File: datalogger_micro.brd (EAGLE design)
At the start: 32 x 40.6 mm, 46 parts, among them IC1 DS3231/SO, IC2 LD117AS33TR, M1 PAT, M2 PAT, Q2 IRLML5203

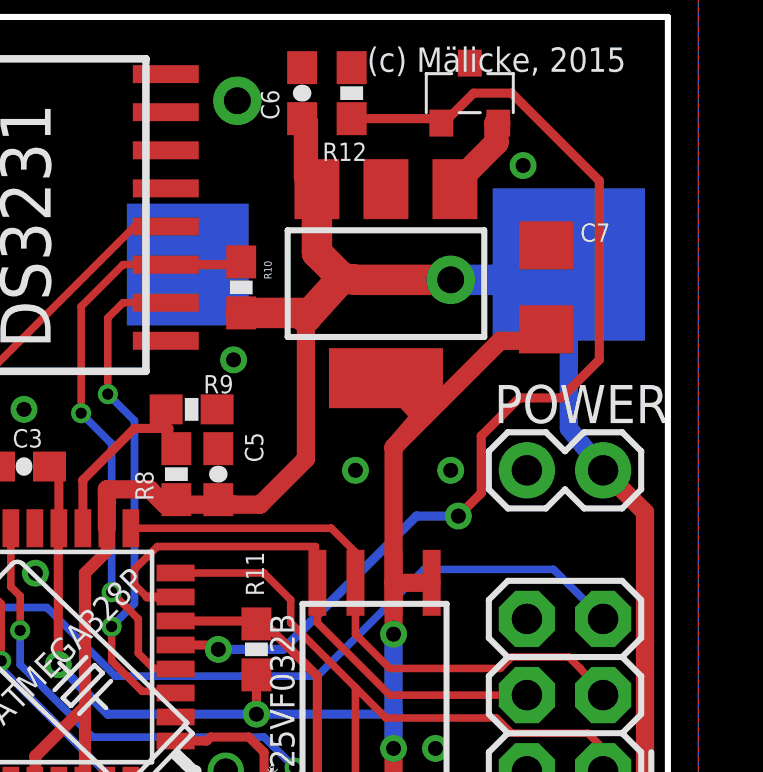
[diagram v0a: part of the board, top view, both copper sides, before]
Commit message: layout error bugfixes
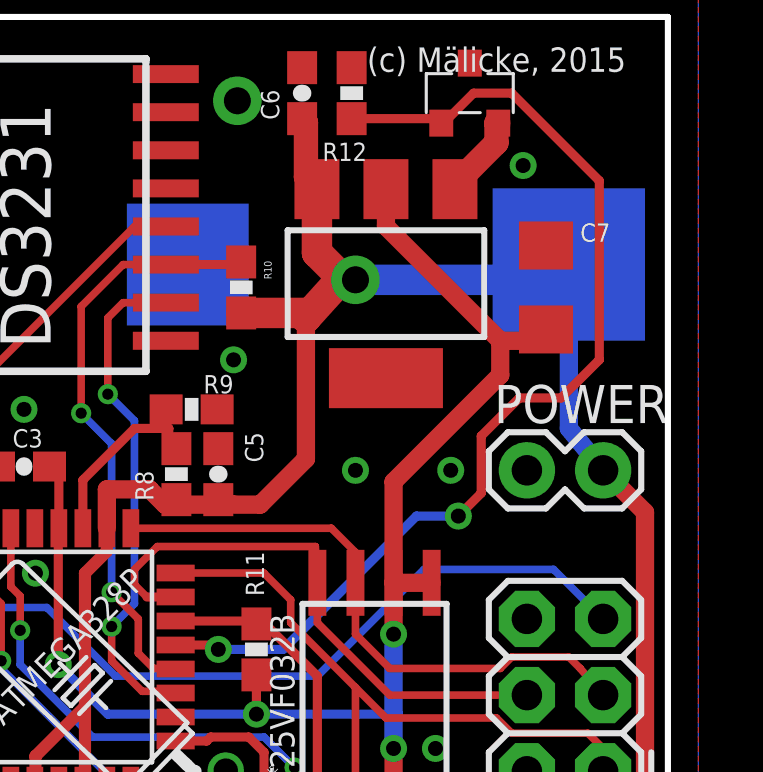
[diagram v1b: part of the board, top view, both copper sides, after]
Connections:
- net VCC-ST: now also IC2.2; no longer IC2.4
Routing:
- net VCC-ST: track 77.0 -> 80.6 mm
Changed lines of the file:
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@@
 <contactref element="R13" pad="1"/>
 <contactref element="R11" pad="1"/>
-<contactref element="IC2" pad="4"/>
+<contactref element="IC2" pad="2"/>
 <contactref element="R18" pad="2"/>
 <contactref element="ATMEGA328P" pad="20"/>
@@
 <wire x1="34.798" y1="9.144" x2="35.179" y2="9.271" width="0.3048" layer="1"/>
 <wire x1="35.179" y1="9.271" x2="35.1481875" y2="9.564" width="0.3048" layer="1"/>
-<wire x1="27.813" y1="23.682" x2="27.813" y2="28.194" width="0.6096" layer="1"/>
-<wire x1="27.813" y1="28.194" x2="31.369" y2="31.75" width="0.6096" layer="1"/>
 <wire x1="31.369" y1="31.75" x2="32.642" y2="31.75" width="0.6096" layer="1"/>
 <wire x1="32.642" y1="31.75" x2="32.893" y2="32.128" width="0.6096" layer="1"/>
-<wire x1="27.813" y1="28.194" x2="28.702" y2="29.235" width="0.6096" layer="1"/>
-<wire x1="28.702" y1="29.235" x2="27.559" y2="30.505" width="0.6096" layer="1"/>
 <wire x1="15.367" y1="7.577" x2="16.51" y2="8.636" width="0.6096" layer="1"/>
 <wire x1="16.51" y1="8.636" x2="27.813" y2="8.636" width="0.6096" layer="1"/>
@@
 <wire x1="16.656" y1="27.882" x2="16.344" y2="27.57" width="0.3048" layer="1"/>
 <wire x1="16.344" y1="27.57" x2="16.344" y2="27.559" width="0.3048" layer="1"/>
+<wire x1="27.559" y1="36.805" x2="27.559" y2="35.56" width="0.6096" layer="1"/>
+<wire x1="27.559" y1="35.56" x2="31.369" y2="31.75" width="0.6096" layer="1"/>
+<wire x1="31.369" y1="31.75" x2="31.369" y2="30.607" width="0.6096" layer="1"/>
+<wire x1="31.369" y1="30.607" x2="27.813" y2="27.051" width="0.6096" layer="1"/>
+<wire x1="27.813" y1="27.051" x2="27.813" y2="23.682" width="0.6096" layer="1"/>
 <wire x1="16.637" y1="25.4826" x2="16.656" y2="25.5016" width="0" layer="19" extent="1-1"/>
 <wire x1="27.813" y1="15.875" x2="27.813" y2="15.942" width="0" layer="19" extent="1-1"/>
@@
 <wire x1="25.259" y1="34.685" x2="26.0985" y2="33.8455" width="1.016" layer="1"/>
 <wire x1="26.0985" y1="33.8455" x2="26.543" y2="33.782" width="1.016" layer="1"/>
-<wire x1="26.543" y1="33.782" x2="29.718" y2="33.782" width="1.016" layer="1"/>
-<via x="29.718" y="33.782" extent="1-16" drill="0.9"/>
-<wire x1="29.718" y1="33.782" x2="33.147" y2="33.782" width="1.016" layer="16"/>
+<via x="26.543" y="33.782" extent="1-16" drill="0.9"/>
+<wire x1="26.543" y1="33.782" x2="33.147" y2="33.782" width="1.016" layer="16"/>
 <wire x1="33.147" y1="33.782" x2="33.655" y2="34.29" width="1.016" layer="16"/>
 <wire x1="22.733" y1="32.678" x2="24.931" y2="32.678" width="1.016" layer="1"/>

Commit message: MOSFET fix
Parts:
- added R19: 100k, SparkFun:0603-RES
- moved M1 17.0 mm to (23.4, 6.60)
- moved M2 17.0 mm to (6.35, 6.48)
- moved VD1 17.0 mm to (25.9, 4.06)
- moved VD2 17.0 mm to (8.89, 3.94)
- moved R12 12.3 mm to (35.1, 31.2)
- moved C6 8.49 mm to (31.8, 35.2)
- moved Q2 8.30 mm to (31.2, 31.8), turned to 90 degrees
- moved C7 6.87 mm to (26.4, 31.2), turned to 180 degrees
- moved R9 5.11 mm to (16.5, 27.2), turned to 270 degrees
- moved R3 4.97 mm to (12.1, 7.90)
- moved IC2 3.97 mm to (27.1, 37.6), turned to 0 degrees
- moved C5 3.27 mm to (18.8, 28.1), turned to 0 degrees
- moved C2 2.93 mm to (9.88, 13.1), turned to 180 degrees
- moved R11 2.11 mm to (22.1, 19.7)
- moved 32.768KHZ 2.11 mm to (20.2, 14.7)
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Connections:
- removed net N$1: IC2.1, Q2.2
- new net N$10: C6.1, IC2.3, Q2.3
- new net N$11: Q2.1, R12.1, R19.2
- net GND: now also IC2.1; no longer Q2.3, R12.2
- net N$5: now also M2.1; no longer M1.1
- net N$6: now also M1.1; no longer M2.1
- net N$8: now also M2.2; no longer M1.2
- net N$9: now also M1.2; no longer M2.2
- net VBAT: now also Q2.2, R19.1; no longer C6.1, IC2.3
- net VCC/ST_ON: now also R12.2; no longer Q2.1, R12.1
- net VDIV1: now also VD1.2; no longer VD2.2
- net VDIV2: now also VD2.2; no longer VD1.2
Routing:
- net VBAT: track 144.4 -> 132.6 mm
- net VCC/ST_ON: track 35.5 -> 24.6 mm
- net DTR: track 8.76 -> 2.52 mm, vias 1 -> 0
- net N$10: track 0.00 -> 6.05 mm
- net VCC-ST: track 80.6 -> 77.1 mm
- net N$11: track 0.00 -> 2.96 mm
- net N$1: track 2.90 -> 0.00 mm
- net RTC_VCC: track 16.8 -> 19.4 mm
- net RTC_RST: track 13.8 -> 16.2 mm
- net VDIV2: track 30.8 -> 28.6 mm
- net SCK: track 20.0 -> 22.1 mm
- net A6: track 6.63 -> 4.54 mm
- net SOIL2: track 23.4 -> 21.4 mm
- net TXO: track 7.61 -> 5.65 mm
- net MOSI: track 18.9 -> 20.8 mm
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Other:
- board text added: "Version 0.96"
- board text removed: "Version 0.95"

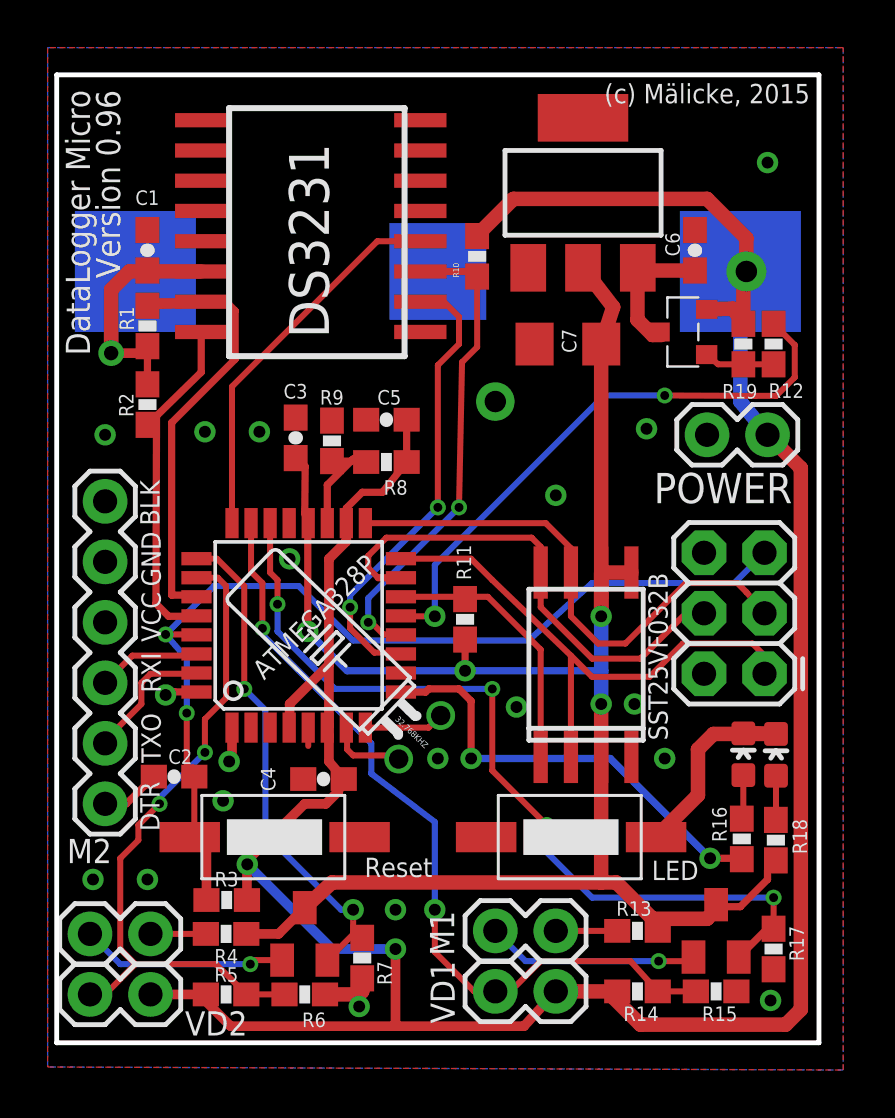
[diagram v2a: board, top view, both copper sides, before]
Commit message: SST25 Layout
pins 5-8 were switched
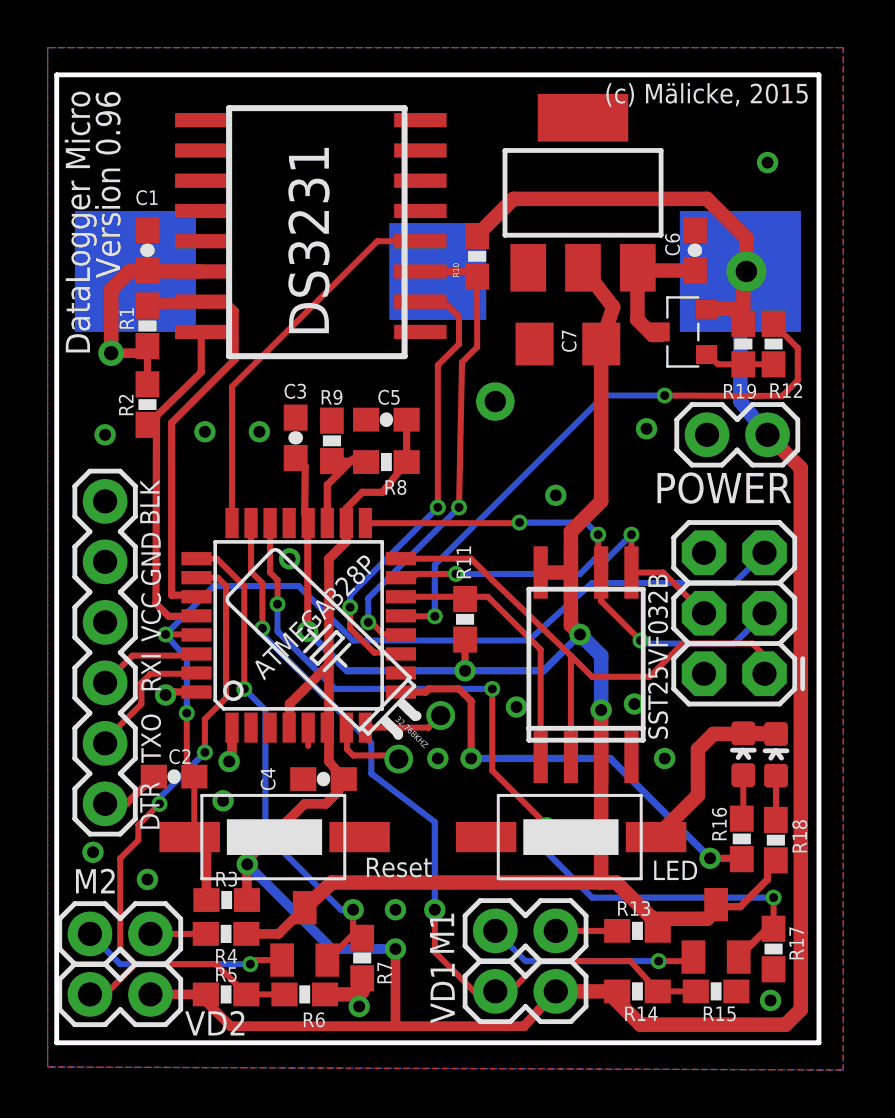
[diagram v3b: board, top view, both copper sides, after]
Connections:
- net MOSI: now also U$3.5; no longer U$3.8
- net SCK: now also U$3.6; no longer U$3.7
- net VCC-ST: now also U$3.7, U$3.8; no longer U$3.5, U$3.6
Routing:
- net MOSI: track 20.8 -> 15.8 mm, vias 0 -> 2
- net SCK: track 22.1 -> 21.0 mm, vias 0 -> 3
- net VCC-ST: track 77.1 -> 76.4 mm
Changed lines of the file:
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@@
 <?xml version="1.0" encoding="utf-8"?>
 <!DOCTYPE eagle SYSTEM "eagle.dtd">
-<eagle version="7.2.0">
+<eagle version="7.3.0">
 <drawing>
 <settings>
@@
 </element>
 <element name="M2" library="SparkFun" package="1X02" value="PAT" x="6.35" y="6.477" smashed="yes">
-<attribute name="NAME" x="5.3848" y="9.4488" size="1.016" layer="25" ratio="10"/>
+<attribute name="NAME" x="5.6388" y="8.1788" size="1.016" layer="25" ratio="10"/>
 <attribute name="VALUE" x="5.08" y="3.302" size="1.27" layer="27"/>
 </element>
@@
 <via x="25.908" y="24.892" extent="1-16" drill="0.5" diameter="0.254"/>
 <contactref element="SPI" pad="6"/>
-<via x="6.477" y="8.763" extent="1-16" drill="0.5" diameter="0.254"/>
+<via x="6.477" y="9.906" extent="1-16" drill="0.5" diameter="0.254"/>
 <wire x1="15.494" y1="15.1574" x2="15.513" y2="15.1384" width="0.254" layer="1"/>
 <via x="11.176" y="27.559" extent="1-16" drill="0.5" diameter="0.254"/>
@@
 </signal>
 <signal name="SCK">
-<contactref element="U$3" pad="7"/>
+<contactref element="U$3" pad="6"/>
 <contactref element="ATMEGA328P" pad="17"/>
-<wire x1="17.913" y1="23.7236" x2="25.4854" y2="23.7236" width="0.254" layer="1"/>
 <contactref element="SPI" pad="3"/>
-<wire x1="34.671" y1="19.939" x2="33.909" y2="20.828" width="0.254" layer="1"/>
-<wire x1="33.909" y1="20.828" x2="33.528" y2="21.209" width="0.254" layer="1"/>
-<wire x1="33.528" y1="21.209" x2="31.369" y2="21.209" width="0.254" layer="1"/>
-<wire x1="31.369" y1="21.209" x2="28.829" y2="18.669" width="0.254" layer="1"/>
-<wire x1="28.829" y1="18.669" x2="27.686" y2="18.669" width="0.254" layer="1"/>
-<wire x1="27.686" y1="18.669" x2="26.543" y2="19.812" width="0.254" layer="1"/>
-<wire x1="26.543" y1="19.812" x2="26.543" y2="21.65" width="0.254" layer="1"/>
-<wire x1="25.4854" y1="23.7236" x2="26.543" y2="22.666" width="0.254" layer="1"/>
-<wire x1="26.543" y1="22.666" x2="26.543" y2="21.65" width="0.254" layer="1"/>
+<wire x1="17.913" y1="23.7236" x2="24.3586" y2="23.7236" width="0.254" layer="1"/>
+<wire x1="24.3586" y1="23.7236" x2="24.384" y2="23.749" width="0.254" layer="1"/>
+<via x="24.384" y="23.749" extent="1-16" drill="0.373"/>
+<wire x1="24.384" y1="23.749" x2="27.178" y2="23.749" width="0.254" layer="16"/>
+<wire x1="27.178" y1="23.749" x2="27.686" y2="23.241" width="0.254" layer="16"/>
+<via x="27.686" y="23.241" extent="1-16" drill="0.373"/>
+<wire x1="27.686" y1="23.241" x2="27.686" y2="21.777" width="0.254" layer="1"/>
+<wire x1="27.686" y1="21.777" x2="27.813" y2="21.65" width="0.254" layer="1"/>
+<wire x1="27.813" y1="21.65" x2="27.813" y2="20.447" width="0.254" layer="1"/>
+<wire x1="27.813" y1="20.447" x2="29.464" y2="18.796" width="0.254" layer="1"/>
+<via x="29.464" y="18.796" extent="1-16" drill="0.373"/>
+<wire x1="29.464" y1="18.796" x2="29.591" y2="18.669" width="0.254" layer="16"/>
+<wire x1="29.591" y1="18.669" x2="33.401" y2="18.669" width="0.254" layer="16"/>
+<wire x1="33.401" y1="18.669" x2="34.671" y2="19.939" width="0.254" layer="16"/>
 </signal>
 <signal name="MISO">
@@
 </signal>
 <signal name="MOSI">
-<contactref element="U$3" pad="8"/>
+<contactref element="U$3" pad="5"/>
 <contactref element="ATMEGA328P" pad="15"/>
-<wire x1="19.4056" y1="21.431" x2="18.447" y2="21.431" width="0.3048" layer="1"/>
-<wire x1="18.447" y1="21.431" x2="18.034" y2="21.844" width="0.254" layer="1"/>
-<wire x1="18.034" y1="21.844" x2="18.034" y2="22.352" width="0.254" layer="1"/>
-<wire x1="18.034" y1="22.352" x2="18.796" y2="23.114" width="0.254" layer="1"/>
-<wire x1="18.796" y1="23.114" x2="24.892" y2="23.114" width="0.254" layer="1"/>
-<wire x1="24.892" y1="23.114" x2="25.273" y2="22.733" width="0.254" layer="1"/>
-<wire x1="25.273" y1="22.733" x2="25.273" y2="21.65" width="0.254" layer="1"/>
 <contactref element="SPI" pad="4"/>
-<wire x1="32.131" y1="19.939" x2="31.369" y2="19.939" width="0.254" layer="1"/>
-<wire x1="31.369" y1="19.939" x2="29.464" y2="18.034" width="0.254" layer="1"/>
-<wire x1="29.464" y1="18.034" x2="27.432" y2="18.034" width="0.254" layer="1"/>
-<wire x1="27.432" y1="18.034" x2="25.273" y2="20.193" width="0.254" layer="1"/>
-<wire x1="25.273" y1="20.193" x2="25.273" y2="21.65" width="0.254" layer="1"/>
+<wire x1="19.4056" y1="21.431" x2="19.907" y2="21.431" width="0.254" layer="1"/>
+<wire x1="19.907" y1="21.431" x2="20.066" y2="21.59" width="0.254" layer="1"/>
+<wire x1="20.066" y1="21.59" x2="21.717" y2="21.59" width="0.254" layer="1"/>
+<via x="21.717" y="21.59" extent="1-16" drill="0.373"/>
+<wire x1="21.717" y1="21.59" x2="26.924" y2="21.59" width="0.254" layer="16"/>
+<wire x1="26.924" y1="21.59" x2="27.559" y2="22.225" width="0.254" layer="16"/>
+<wire x1="27.559" y1="22.225" x2="28.067" y2="22.225" width="0.254" layer="16"/>
+<wire x1="28.067" y1="22.225" x2="29.083" y2="23.241" width="0.254" layer="16"/>
+<via x="29.083" y="23.241" extent="1-16" drill="0.373"/>
+<wire x1="29.083" y1="23.241" x2="29.083" y2="21.65" width="0.254" layer="1"/>
+<wire x1="29.083" y1="21.65" x2="30.42" y2="21.65" width="0.254" layer="1"/>
+<wire x1="30.42" y1="21.65" x2="32.131" y2="19.939" width="0.254" layer="1"/>
 </signal>
 <signal name="N$7">
@@
 <signal name="VCC-ST">
 <contactref element="U$3" pad="3"/>
-<contactref element="U$3" pad="5"/>
-<contactref element="U$3" pad="6"/>
+<contactref element="U$3" pad="8"/>
+<contactref element="U$3" pad="7"/>
 <contactref element="Q3" pad="3"/>
 <contactref element="R13" pad="1"/>
@@
 <wire x1="15.367" y1="24.13" x2="15.513" y2="23.7236" width="0.3048" layer="1"/>
 <via x="22.098" y="17.526" extent="1-16" drill="0.5"/>
-<wire x1="29.083" y1="21.65" x2="27.813" y2="21.65" width="0.6096" layer="1"/>
-<wire x1="27.813" y1="21.65" x2="27.813" y2="19.812" width="0.6096" layer="1"/>
-<via x="27.813" y="19.812" extent="1-16" drill="0.5"/>
 <wire x1="12.915" y1="6.477" x2="14.267" y2="6.477" width="0.4064" layer="1"/>
 <wire x1="14.267" y1="6.477" x2="15.367" y2="7.577" width="0.4064" layer="1"/>
-<wire x1="27.813" y1="19.812" x2="27.813" y2="17.526" width="0.6096" layer="16"/>
-<via x="27.813" y="16.129" extent="1-16" drill="0.5"/>
-<wire x1="27.813" y1="17.526" x2="27.813" y2="16.129" width="0.6096" layer="16"/>
-<wire x1="27.813" y1="16.129" x2="27.813" y2="13.91" width="0.6096" layer="1"/>
-<wire x1="22.098" y1="17.526" x2="27.813" y2="17.526" width="0.3048" layer="16"/>
-<wire x1="22.098" y1="18.835" x2="22.098" y2="17.526" width="0.3048" layer="1"/>
 <wire x1="27.813" y1="13.843" x2="27.813" y2="8.636" width="0.6096" layer="1"/>
 <wire x1="32.639" y1="7.704" x2="32.766" y2="7.62" width="0.3048" layer="1"/>
@@
 <wire x1="28.318" y1="32.794" x2="27.816" y2="31.242" width="0.6096" layer="1"/>
 <wire x1="27.816" y1="31.242" x2="27.813" y2="30.858" width="0.6096" layer="1"/>
-<wire x1="27.813" y1="30.858" x2="27.813" y2="19.812" width="0.6096" layer="1"/>
-<wire x1="15.494" y1="23.7046" x2="15.513" y2="23.7236" width="0" layer="19" extent="1-1"/>
+<wire x1="27.813" y1="13.91" x2="27.813" y2="15.875" width="0.6096" layer="1"/>
+<via x="27.813" y="15.875" extent="1-16" drill="0.5"/>
+<wire x1="27.813" y1="15.875" x2="27.813" y2="18.161" width="0.6096" layer="16"/>
+<wire x1="27.813" y1="18.161" x2="26.924" y2="19.05" width="0.6096" layer="16"/>
+<via x="26.924" y="19.05" extent="1-16" drill="0.5"/>
+<wire x1="26.924" y1="19.05" x2="26.543" y2="19.431" width="0.6096" layer="1"/>
+<wire x1="26.543" y1="19.431" x2="26.543" y2="21.65" width="0.6096" layer="1"/>
+<wire x1="26.543" y1="21.65" x2="25.273" y2="21.65" width="0.6096" layer="1"/>
+<wire x1="26.543" y1="21.65" x2="26.543" y2="23.368" width="0.6096" layer="1"/>
+<wire x1="26.543" y1="23.368" x2="27.813" y2="24.638" width="0.6096" layer="1"/>
+<wire x1="27.813" y1="24.638" x2="27.813" y2="31.239" width="0.6096" layer="1"/>
+<wire x1="27.813" y1="31.239" x2="27.816" y2="31.242" width="0.6096" layer="1"/>
+<wire x1="22.098" y1="17.526" x2="25.4" y2="17.526" width="0.3048" layer="16"/>
+<wire x1="25.4" y1="17.526" x2="26.924" y2="19.05" width="0.3048" layer="16"/>
+<wire x1="15.513" y1="23.7236" x2="15.494" y2="23.7046" width="0" layer="19" extent="1-1"/>
 <wire x1="27.813" y1="13.843" x2="27.813" y2="13.91" width="0" layer="19" extent="1-1"/>
+<wire x1="22.098" y1="17.526" x2="22.098" y2="18.835" width="0.3048" layer="1"/>
 </signal>
 <signal name="VCC/ST_ON">
 <contactref element="ATMEGA328P" pad="13"/>
 <via x="30.48" y="29.083" extent="1-16" drill="0.373"/>
-<via x="20.828" y="19.812" extent="1-16" drill="0.5"/>
+<via x="20.828" y="19.812" extent="1-16" drill="0.373"/>
 <wire x1="20.828" y1="19.812" x2="19.4246" y2="19.812" width="0.254" layer="1"/>
 <wire x1="19.4246" y1="19.812" x2="19.4056" y2="19.831" width="0.254" layer="1"/>
@@
 <wire x1="20.828" y1="19.812" x2="20.828" y2="21.971" width="0.254" layer="16"/>
 <contactref element="R12" pad="2"/>
-<wire x1="34.274" y1="29.067" x2="35.163" y2="29.067" width="0.254" layer="1"/>
-<wire x1="35.163" y1="29.067" x2="35.941" y2="29.845" width="0.254" layer="1"/>
-<wire x1="35.941" y1="29.845" x2="35.941" y2="31.203" width="0.254" layer="1"/>
-<wire x1="35.941" y1="31.203" x2="35.052" y2="32.092" width="0.254" layer="1"/>
+<wire x1="34.274" y1="29.067" x2="35.417" y2="29.067" width="0.254" layer="1"/>
+<wire x1="35.417" y1="29.067" x2="36.068" y2="29.718" width="0.254" layer="1"/>
+<wire x1="36.068" y1="29.718" x2="36.068" y2="31.076" width="0.254" layer="1"/>
+<wire x1="36.068" y1="31.076" x2="35.052" y2="32.092" width="0.254" layer="1"/>
 <wire x1="20.828" y1="21.971" x2="27.94" y2="29.083" width="0.254" layer="16"/>
 <wire x1="27.94" y1="29.083" x2="30.48" y2="29.083" width="0.254" layer="16"/>
